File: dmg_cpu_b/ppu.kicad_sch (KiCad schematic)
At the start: 0 parts

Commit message: Minor tweaks to help with clarity.
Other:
- added sheet OAM (oam.kicad_sch)
- sheet FF46 DMA ports: added OAM_PHI, OAM_WR; removed CPU_PHI2, WYJA
- sheet PPU DECODE ports: added CPU_PHI2, OAM_PHI; removed none
- sheet VRAM INTERFACE ports: added RAM_CS_EN, T1~{T2}; removed ABUZ, ~{T1}T2
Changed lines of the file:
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@@
+      (effects (font (size 1.27 1.27)) (justify left))
+    )
+    (pin "CPU_PHI2" input (at 32.385 32.385 180)
+      (effects (font (size 1.27 1.27)) (justify left))
+    )
+    (pin "OAM_PHI" output (at 54.61 34.29 270)
       (effects (font (size 1.27 1.27)) (justify left))
     )
@@
     )
     (pin "FF46" input (at 64.77 59.69 180)
-      (effects (font (size 1.27 1.27)) (justify left))
-    )
-    (pin "CPU_PHI2" input (at 64.77 65.405 180)
       (effects (font (size 1.27 1.27)) (justify left))
     )
@@
       (effects (font (size 1.27 1.27)) (justify right))
     )
-    (pin "WYJA" output (at 104.14 64.135 0)
-      (effects (font (size 1.27 1.27)) (justify right))
-    )
     (pin "DMA_A[0..15]" output (at 104.14 67.945 0)
       (effects (font (size 1.27 1.27)) (justify right))
@@
     (pin "PPU_WR" input (at 64.77 55.88 180)
       (effects (font (size 1.27 1.27)) (justify left))
+    )
+    (pin "OAM_PHI" input (at 64.77 65.405 180)
+      (effects (font (size 1.27 1.27)) (justify left))
+    )
+    (pin "OAM_WR" output (at 104.14 64.135 0)
+      (effects (font (size 1.27 1.27)) (justify right))
+    )
+  )
+  (sheet (at 64.77 135.89) (size 28.575 36.195) (fields_autoplaced)
+    (stroke (width 0.1524) (type solid) (color 0 0 0 0))
+    (fill (color 0 0 0 0.0000))
+    (property "Sheet name" "OAM" (id 0) (at 64.77 135.1784 0)
+      (effects (font (size 1.27 1.27)) (justify left bottom))
+    )
+    (property "Sheet file" "oam.kicad_sch" (id 1) (at 64.77 172.6696 0)
+      (effects (font (size 1.27 1.27)) (justify left top))
     )
   )
@@
       (effects (font (size 1.27 1.27)) (justify left))
     )
-    (pin "ABUZ" input (at 64.77 112.395 180)
+    (pin "RAM_CS_EN" input (at 64.77 112.395 180)
       (effects (font (size 1.27 1.27)) (justify left))
     )
@@
       (effects (font (size 1.27 1.27)) (justify left))
     )
-    (pin "~{T1}T2" input (at 64.77 104.775 180)
+    (pin "T1~{T2}" input (at 64.77 104.775 180)
       (effects (font (size 1.27 1.27)) (justify left))
     )

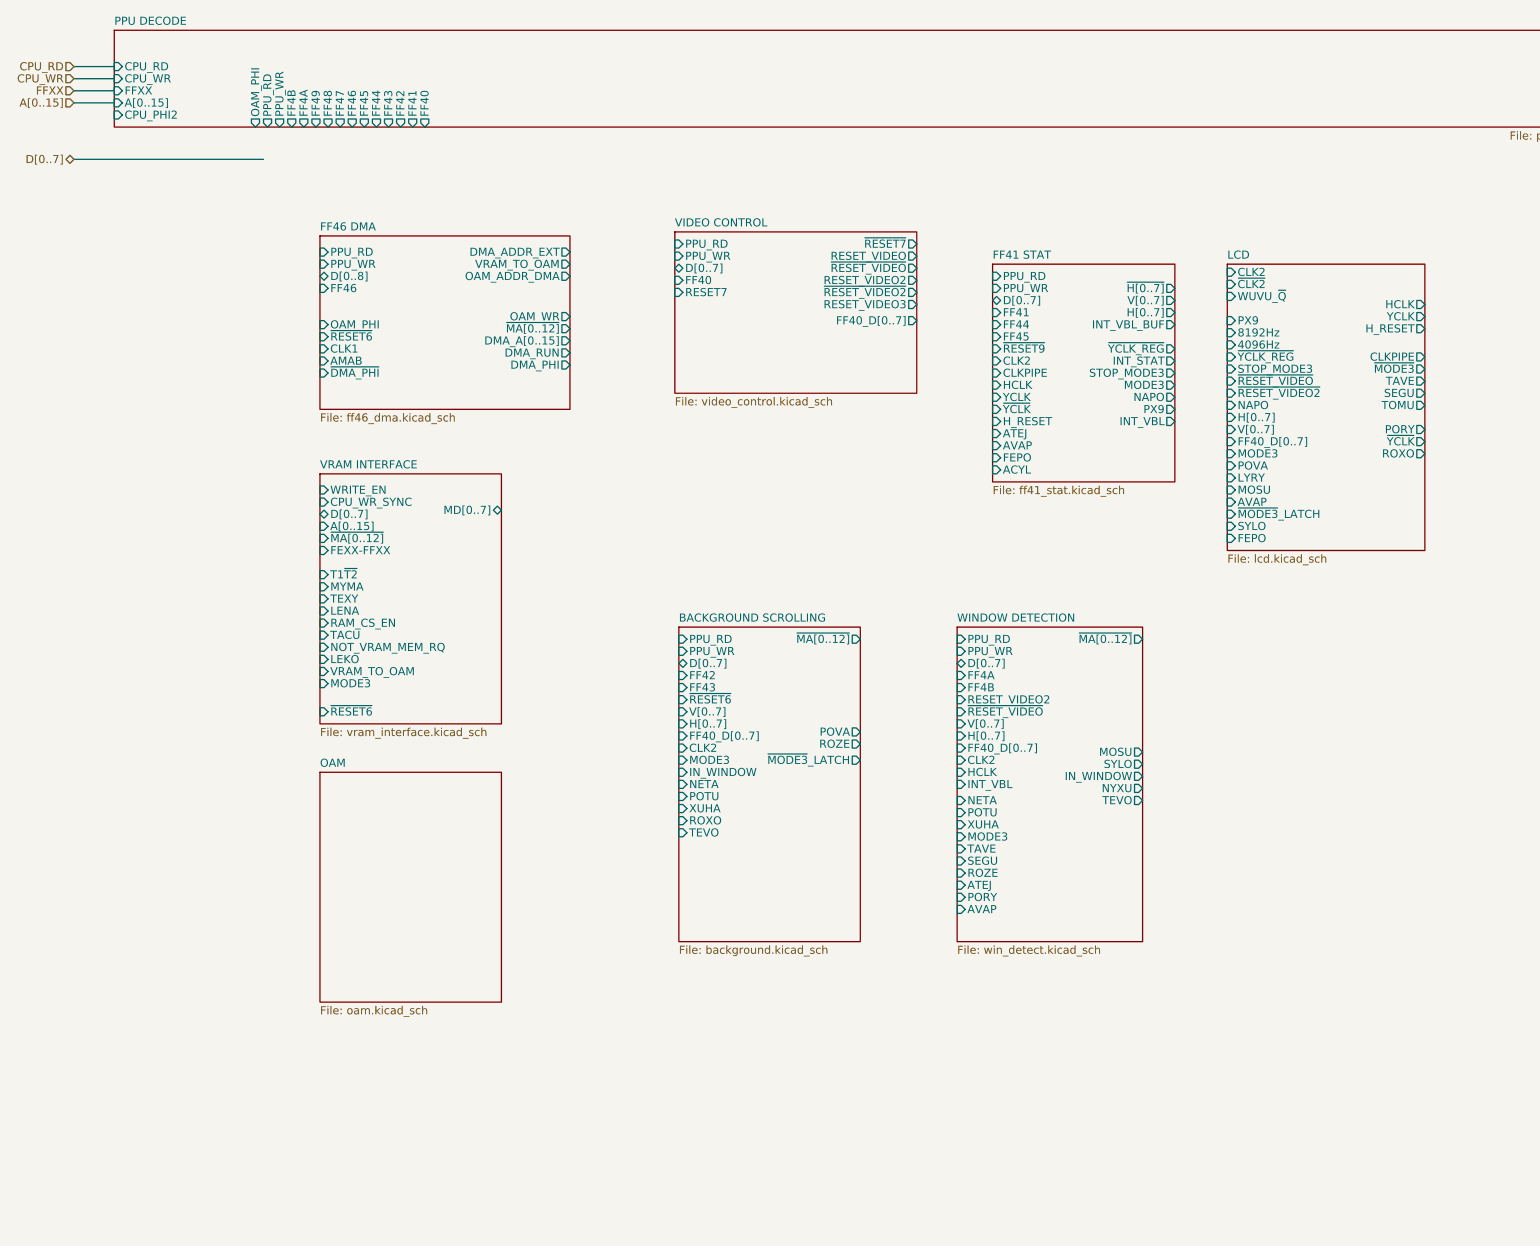
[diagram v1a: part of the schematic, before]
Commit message: OAM and sprite x priority sheets added. OAM sheet still needs some work on it.
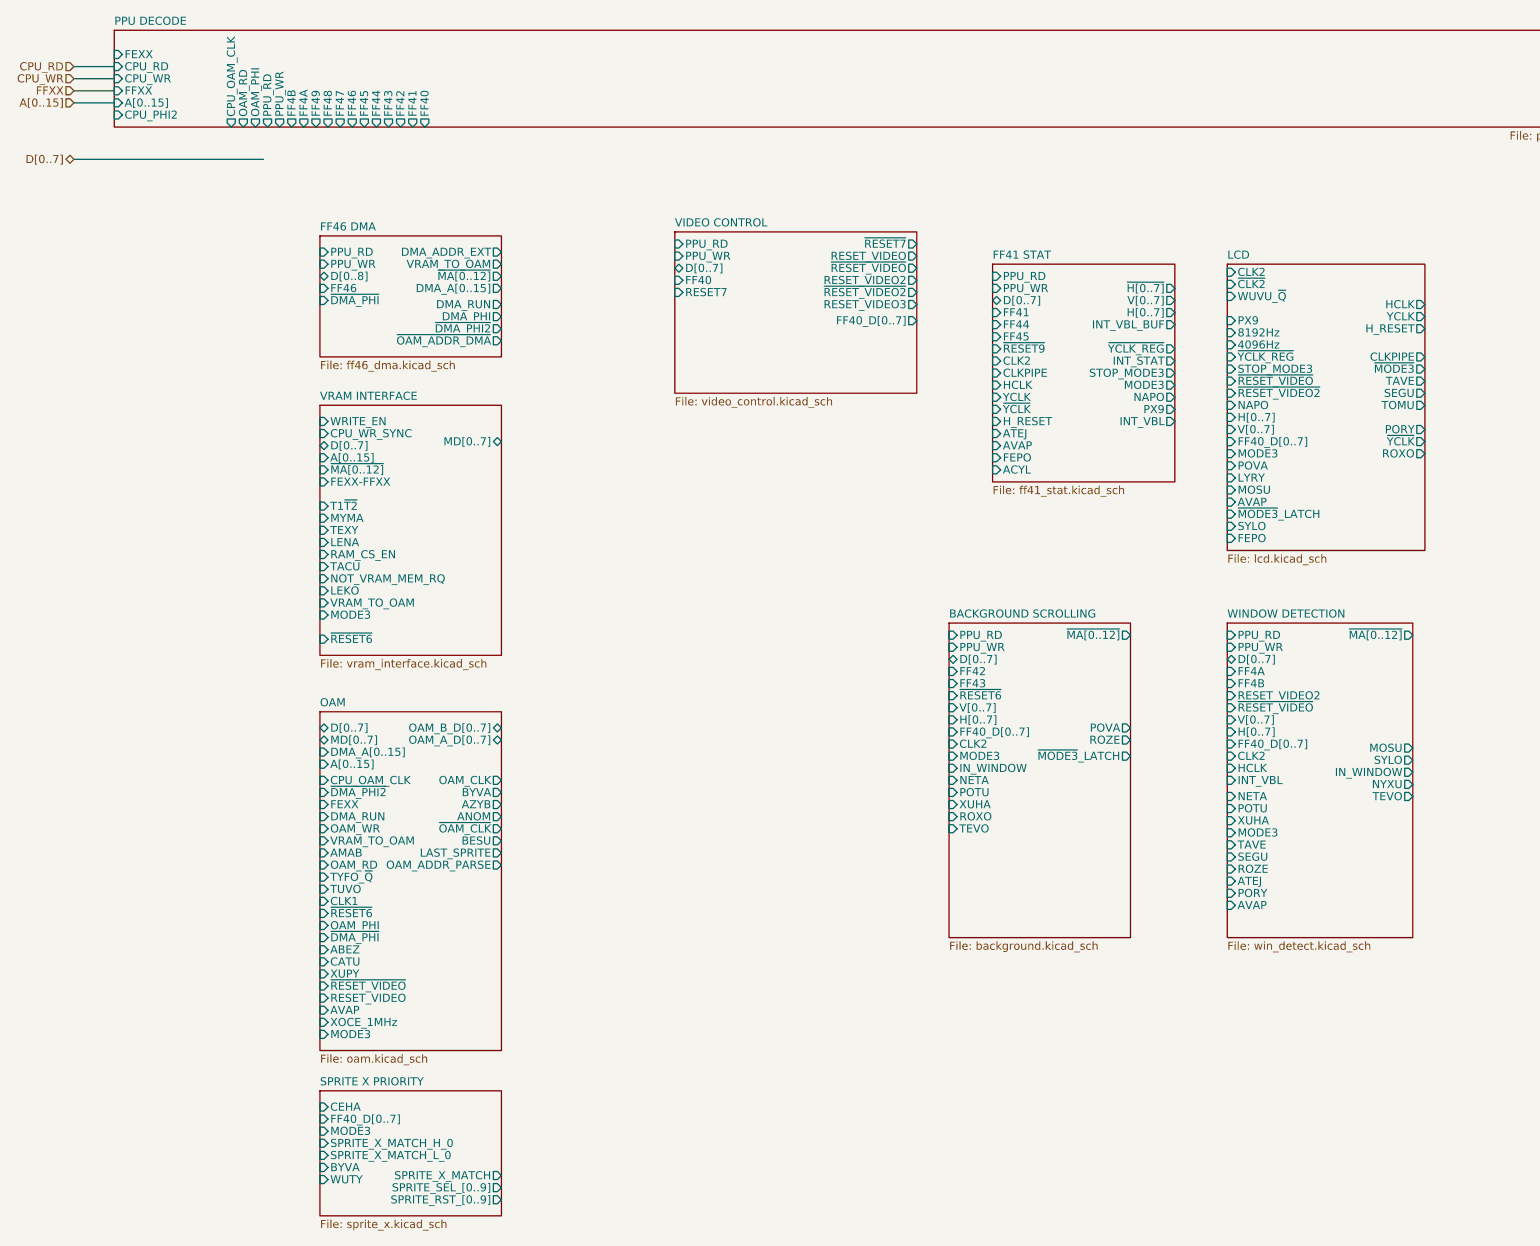
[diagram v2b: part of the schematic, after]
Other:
- added sheet SPRITE X PRIORITY (sprite_x.kicad_sch)
- sheet FF46 DMA ports: added ~{DMA_PHI2}, ~{OAM_ADDR_DMA}; removed AMAB, CLK1, OAM_ADDR_DMA, OAM_PHI, OAM_WR, ~{RESET6}
- sheet OAM ports: added ABEZ, AMAB, ANOM, AVAP, AZYB, A[0..15], BESU, BYVA, CATU, CLK1, CPU_OAM_CLK, DMA_A[0..15], DMA_RUN, D[0..7], FEXX, LAST_SPRITE, MD[0..7], MODE3, OAM_ADDR_PARSE, OAM_A_D[0..7], OAM_B_D[0..7], OAM_CLK, OAM_PHI, OAM_RD, OAM_WR, RESET_VIDEO, TUVO, TYFO_~{Q}, VRAM_TO_OAM, XOCE_1MHz, XUPY, ~{DMA_PHI2}, ~{DMA_PHI}, ~{OAM_CLK}, ~{RESET6}, ~{RESET_VIDEO}; removed none
- sheet PPU DECODE ports: added CPU_OAM_CLK, FEXX, OAM_RD; removed none

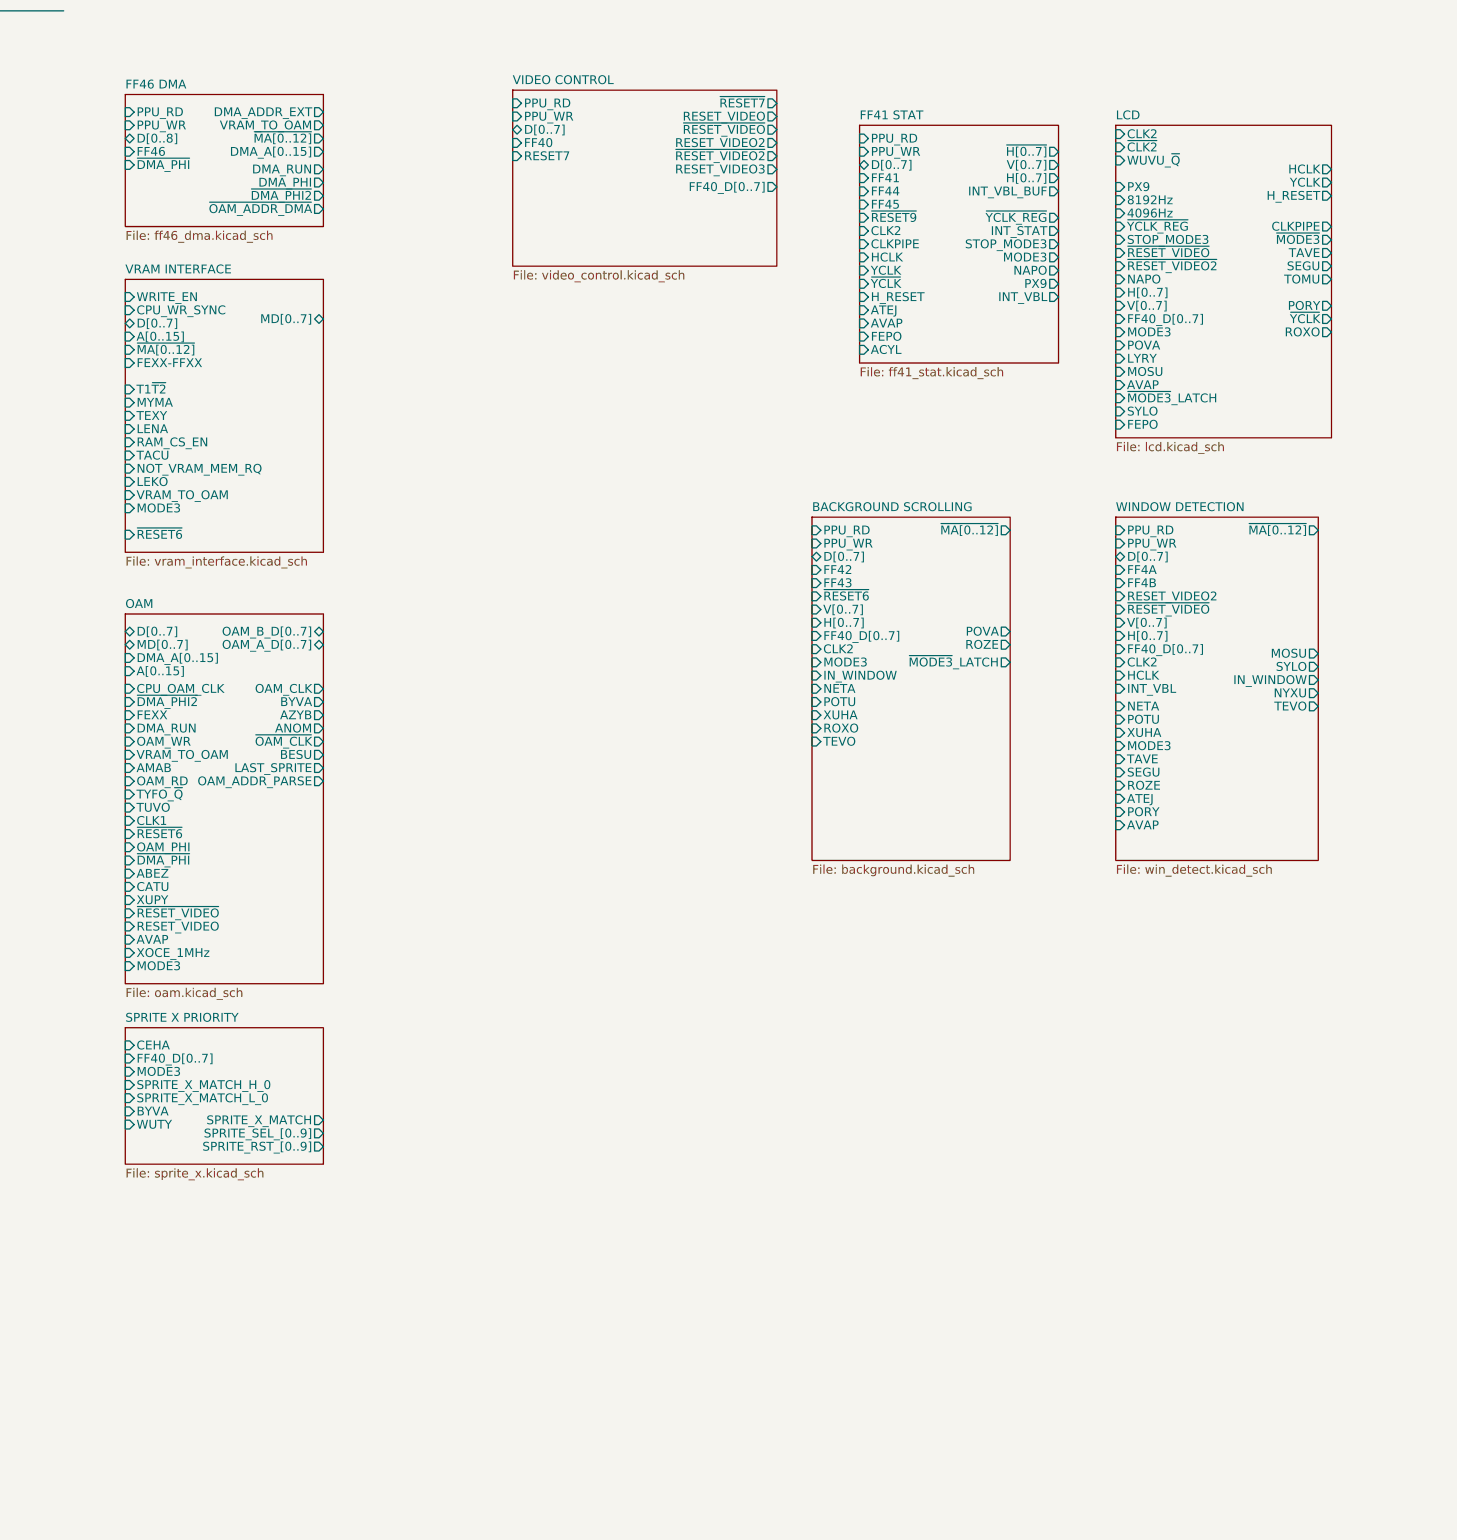
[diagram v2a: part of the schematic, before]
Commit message: sprite y comparator added
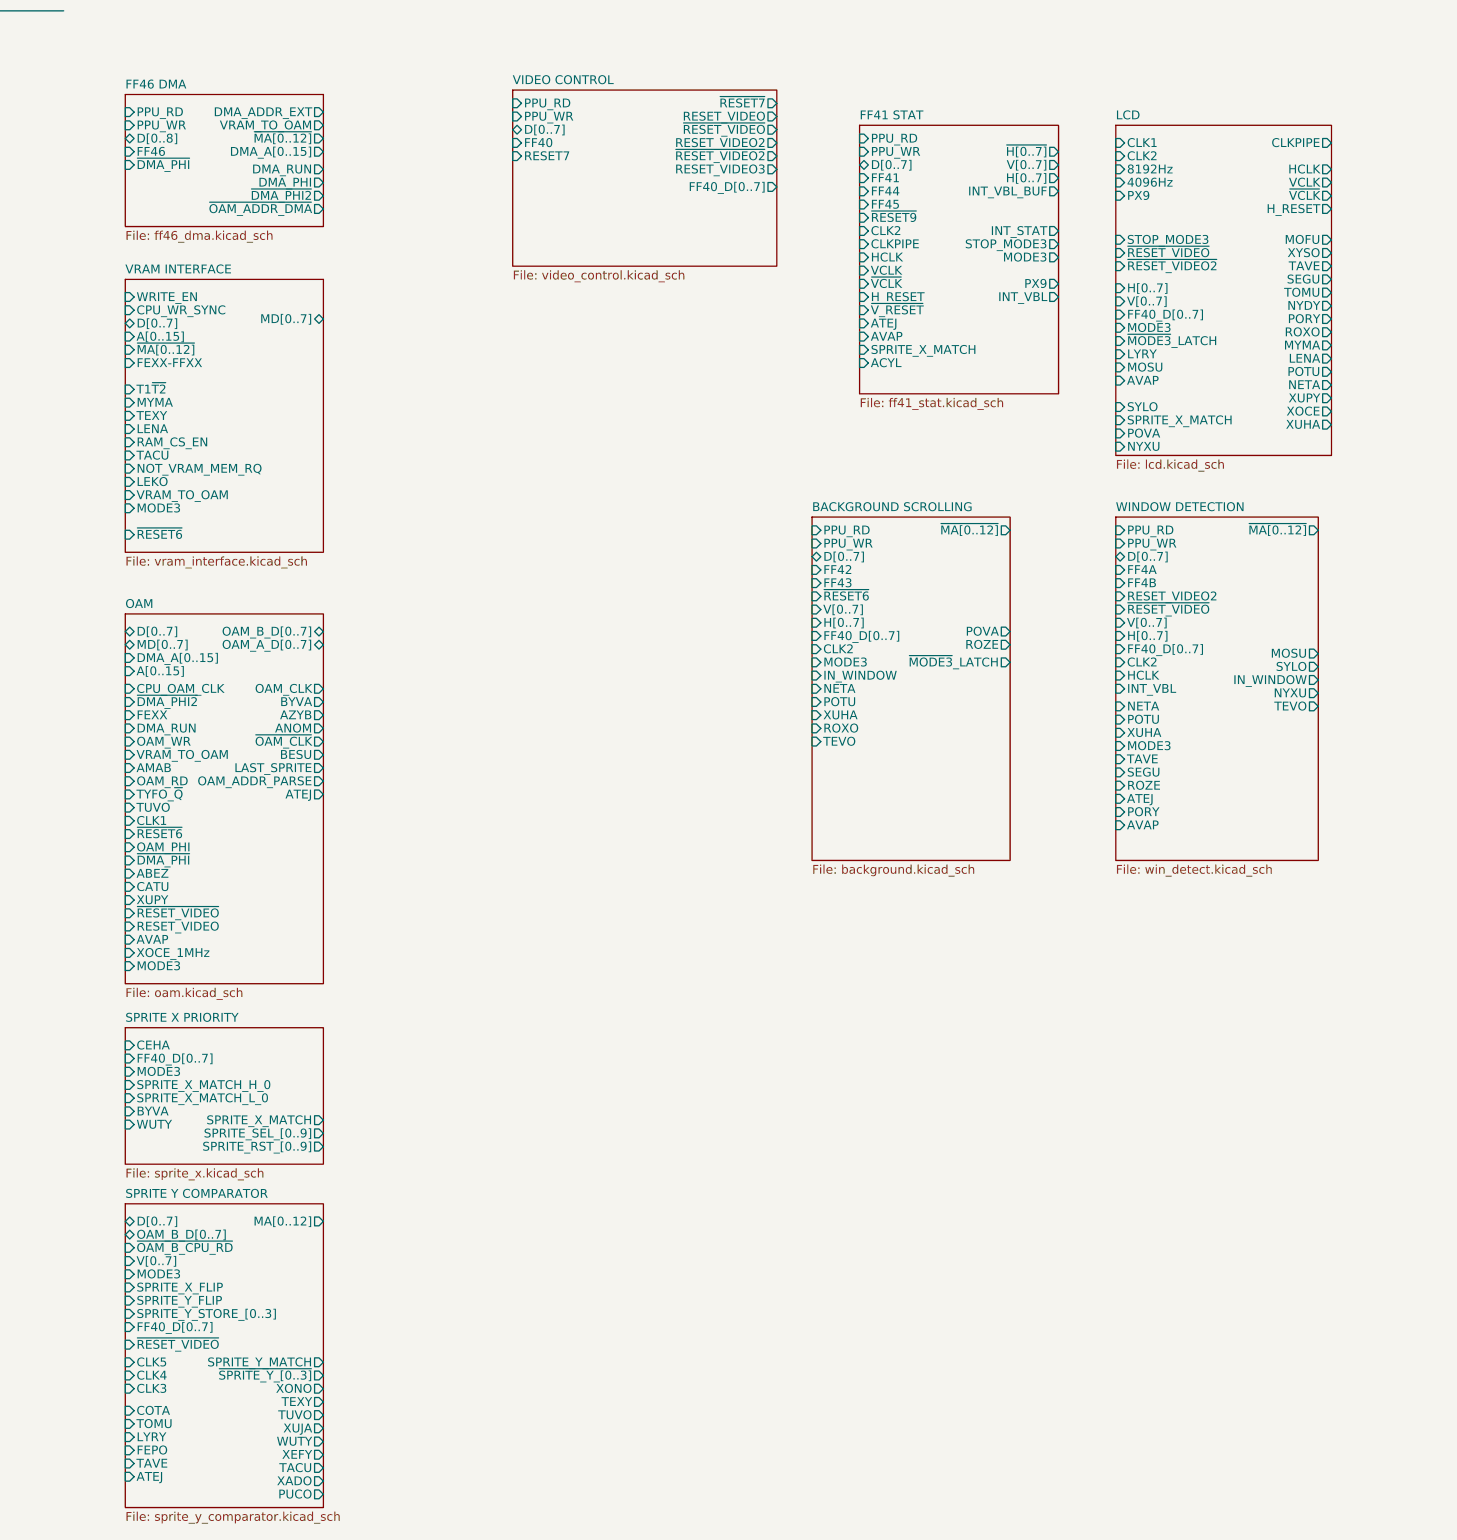
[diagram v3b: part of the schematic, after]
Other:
- added sheet SPRITE Y COMPARATOR (sprite_y_comparator.kicad_sch)
- sheet FF41 STAT ports: added SPRITE_X_MATCH, VCLK, ~{VCLK}, ~{V_RESET}; removed FEPO, NAPO, YCLK, ~{YCLK_REG}, ~{YCLK}
- sheet LCD ports: added CLK1, LENA, MOFU, MYMA, NETA, NYDY, NYXU, POTU, SPRITE_X_MATCH, VCLK, XOCE, XUHA, XUPY, XYSO, ~{VCLK}; removed FEPO, NAPO, WUVU_~{Q}, YCLK, ~{CLK2}, ~{MODE3}, ~{YCLK_REG}, ~{YCLK}
- sheet OAM ports: added ATEJ; removed none
